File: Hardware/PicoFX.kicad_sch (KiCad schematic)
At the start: 11 parts, among them J1 RPI_ADC, J2 RP_GPIO

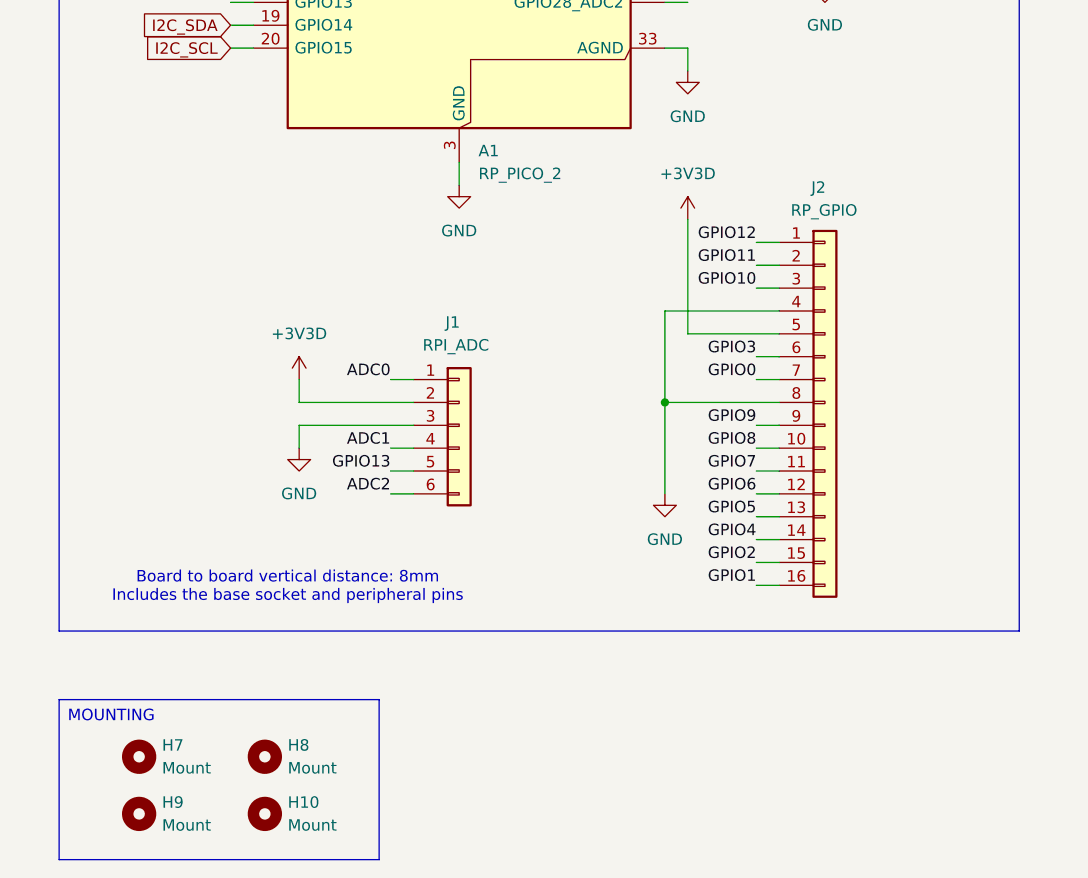
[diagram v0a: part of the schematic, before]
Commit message: Layout revision
Minor updated to references.
Minor updated to the PCB layout.
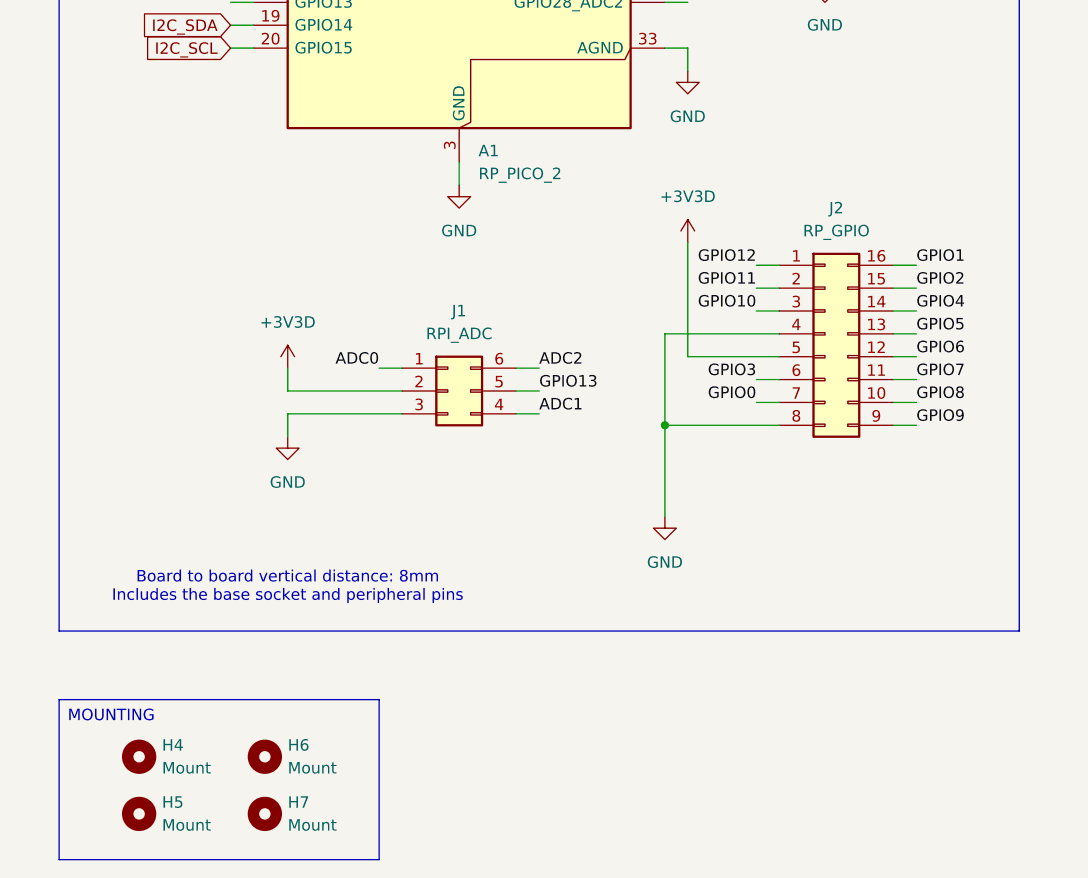
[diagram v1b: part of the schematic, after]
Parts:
- removed J1: RPI_ADC, Custom_Parts:HEADER_THROUGH_2x03_P2.54mm, symbol Connector_Generic:Conn_01x06
- removed J2: RP_GPIO, Custom_Parts:HEADER_THROUGH_2x08_P2.54mm, symbol Connector_Generic:Conn_01x16
- added J1: RPI_ADC, Custom_Parts:HEADER_THROUGH_2x03_P2.54mm, symbol Connector_Generic:Conn_02x03_Counter_Clockwise
- added J2: RP_GPIO, Custom_Parts:HEADER_THROUGH_2x08_P2.54mm, symbol Connector_Generic:Conn_02x08_Counter_Clockwise
- renumbered H7 to H4, H9 to H5, H8 to H6, H10 to H7
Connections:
- net +3V3D: now also J1.2 (Pin_2), J2.5 (Pin_5)
- net ADC0: now also J1.1 (Pin_1)
- net ADC1: now also J1.4 (Pin_4)
- net ADC2: now also J1.6 (Pin_6)
- net GND: now also J1.3 (Pin_3), J2.4 (Pin_4), J2.8 (Pin_8)
- net GPIO0: now also J2.7 (Pin_7)
- net GPIO1: now also J2.16 (Pin_16)
- net GPIO10: now also J2.3 (Pin_3)
- net GPIO11: now also J2.2 (Pin_2)
- net GPIO12: now also J2.1 (Pin_1)
- net GPIO13: now also J1.5 (Pin_5)
- net GPIO2: now also J2.15 (Pin_15)
- net GPIO3: now also J2.6 (Pin_6)
- net GPIO4: now also J2.14 (Pin_14)
- net GPIO5: now also J2.13 (Pin_13)
- net GPIO6: now also J2.12 (Pin_12)
- net GPIO7: now also J2.11 (Pin_11)
- net GPIO8: now also J2.10 (Pin_10)
- net GPIO9: now also J2.9 (Pin_9)
